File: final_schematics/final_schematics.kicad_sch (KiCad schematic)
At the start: 0 parts

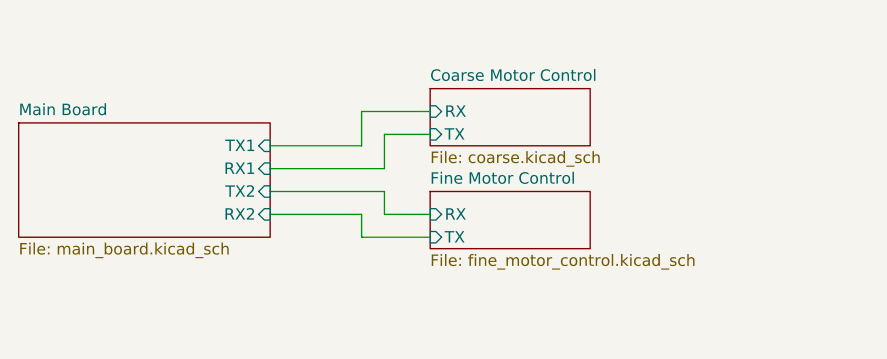
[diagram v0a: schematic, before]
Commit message: Test code on main board
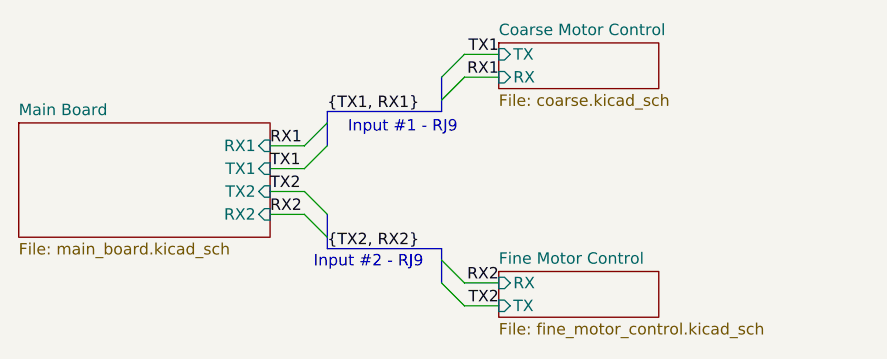
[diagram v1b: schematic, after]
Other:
- note added: "Input #1 - RJ9"
- note added: "Input #2 - RJ9"
